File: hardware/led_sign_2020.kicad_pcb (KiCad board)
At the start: 2 copper layers, 70 x 86 mm, 30 parts, among them Q1 STD26P3LLH6, U1 ESP32-DevKitC, U2 MC74VHC1GT125, U3 MC74VHC1GT125, U4 MAX17601, U5 MAX17601, U6 MAX17601, U7 MAX17601

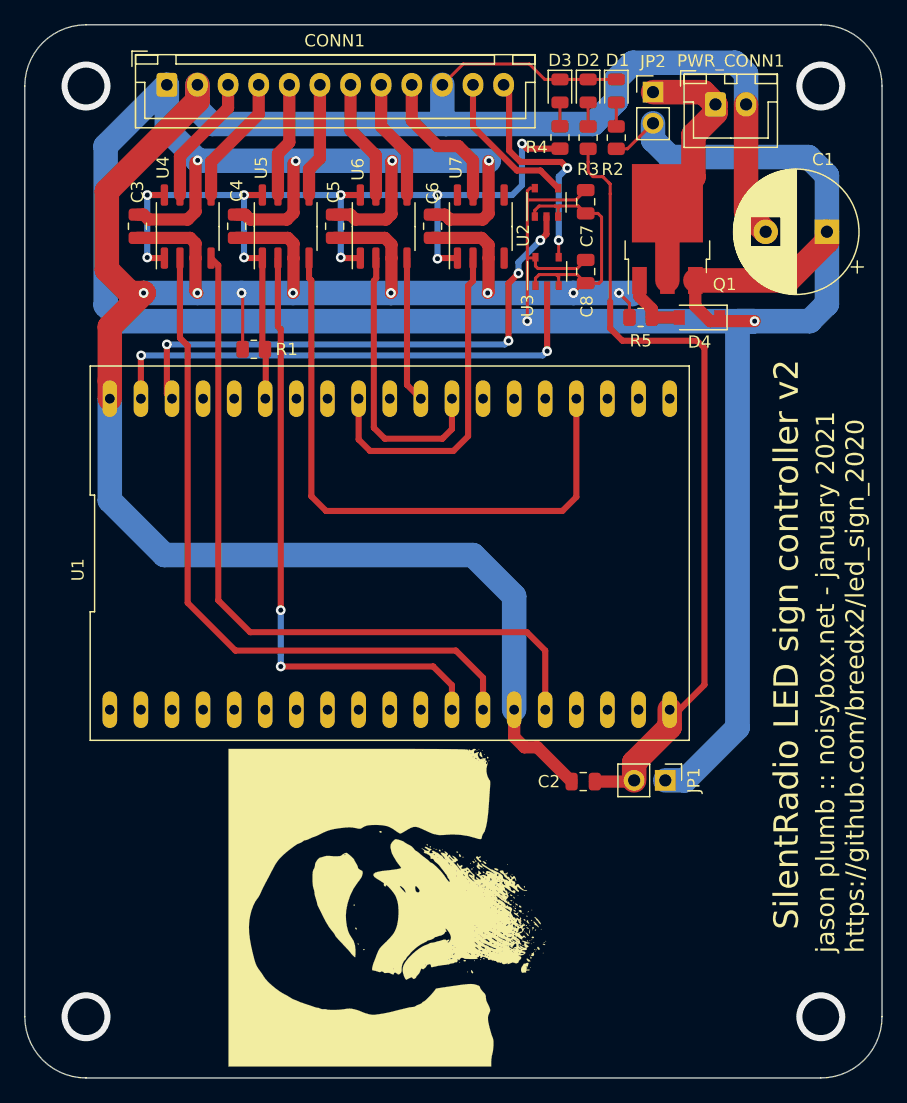
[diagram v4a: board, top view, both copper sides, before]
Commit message: add test point and silk notes
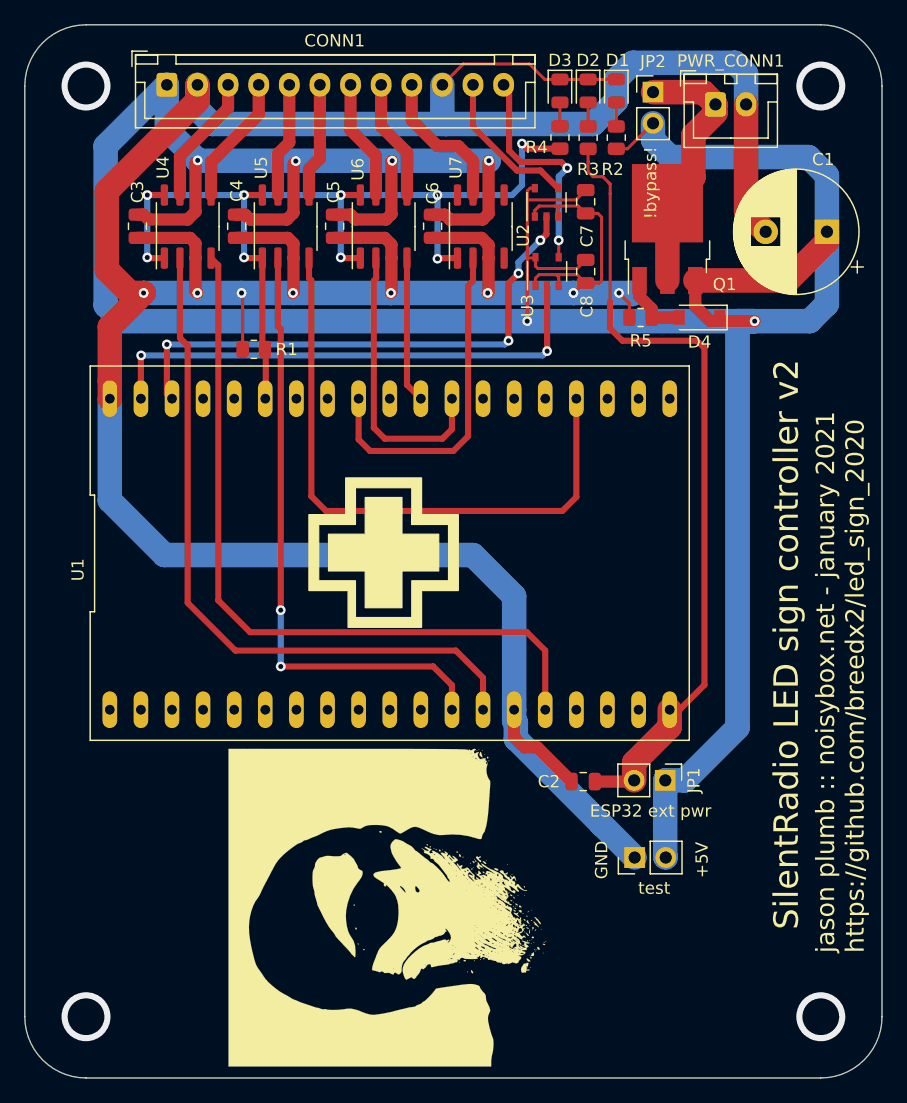
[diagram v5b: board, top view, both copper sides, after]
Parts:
- added test: PinHeader_1x02_P2.54mm_Vertical, Connector_PinHeader_2.54mm:PinHeader_1x02_P2.54mm_Vertical, F.Cu at (124.8, 123.0)
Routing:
- net GND: track 281.0 -> 297.2 mm
- net +5V: track 266.0 -> 272.3 mm
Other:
- board text added: "!bypass!"
- board text added: "+5V"
- board text added: "ESP32 ext pwr"
- board text added: "GND"
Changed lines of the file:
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@@
   (general
     (thickness 1.6)
-    (drawings 10)
-    (tracks 358)
+    (drawings 17)
+    (tracks 365)
     (zones 0)
-    (modules 30)
+    (modules 31)
     (nets 28)
   )
   (page A4)
   (layers
-    (0 F.Cu signal)
-    (31 B.Cu signal)
+    (0 F.Cu signal hide)
+    (31 B.Cu signal hide)
     (32 B.Adhes user)
     (33 F.Adhes user)
@@
     (38 B.Mask user)
     (39 F.Mask user)
-    (40 Dwgs.User user hide)
+    (40 Dwgs.User user)
     (41 Cmts.User user)
     (42 Eco1.User user)
@@
   )
   (setup
-    (last_trace_width 0.25)
+    (last_trace_width 2)
     (user_trace_width 0.25)
     (user_trace_width 0.5)
@@
     (mod_text_size 1 1)
     (mod_text_width 0.15)
-    (pad_size 1.524 1.524)
-    (pad_drill 0.762)
+    (pad_size 1.7 1.7)
+    (pad_drill 1)
     (pad_to_mask_clearance 0.0508)
     (solder_mask_min_width 0.101)
@@
     (add_net "Net-(D4-Pad2)")
     (add_net "Net-(JP2-Pad1)")
+  )
+  (module Connector_PinHeader_2.54mm:PinHeader_1x02_P2.54mm_Vertical (layer F.Cu)
+    (at 124.8 123 90)
+    (descr "Through hole straight pin header, 1x02, 2.54mm pitch, single row")
+    (tags "Through hole pin header THT 1x02 2.54mm single row")
+    (fp_text reference test (at -2.5 1.6 180) (layer F.SilkS)
+      (effects (font (size 1 1) (thickness 0.15)))
+    )
+    (fp_text value PinHeader_1x02_P2.54mm_Vertical (at 0 4.87 90) (layer F.Fab)
+      (effects (font (size 1 1) (thickness 0.15)))
+    )
+    (fp_line (start 1.8 -1.8) (end -1.8 -1.8) (layer F.CrtYd) (width 0.05))
+    (fp_line (start 1.8 4.35) (end 1.8 -1.8) (layer F.CrtYd) (width 0.05))
+    (fp_line (start -1.8 4.35) (end 1.8 4.35) (layer F.CrtYd) (width 0.05))
+    (fp_line (start -1.8 -1.8) (end -1.8 4.35) (layer F.CrtYd) (width 0.05))
+    (fp_line (start -1.33 -1.33) (end 0 -1.33) (layer F.SilkS) (width 0.12))
+    (fp_line (start -1.33 0) (end -1.33 -1.33) (layer F.SilkS) (width 0.12))
+    (fp_line (start -1.33 1.27) (end 1.33 1.27) (layer F.SilkS) (width 0.12))
+    (fp_line (start 1.33 1.27) (end 1.33 3.87) (layer F.SilkS) (width 0.12))
+    (fp_line (start -1.33 1.27) (end -1.33 3.87) (layer F.SilkS) (width 0.12))
+    (fp_line (start -1.33 3.87) (end 1.33 3.87) (layer F.SilkS) (width 0.12))
+    (fp_line (start -1.27 -0.635) (end -0.635 -1.27) (layer F.Fab) (width 0.1))
+    (fp_line (start -1.27 3.81) (end -1.27 -0.635) (layer F.Fab) (width 0.1))
+    (fp_line (start 1.27 3.81) (end -1.27 3.81) (layer F.Fab) (width 0.1))
+    (fp_line (start 1.27 -1.27) (end 1.27 3.81) (layer F.Fab) (width 0.1))
+    (fp_line (start -0.635 -1.27) (end 1.27 -1.27) (layer F.Fab) (width 0.1))
+    (fp_text user %R (at 0 1.27) (layer F.Fab)
+      (effects (font (size 1 1) (thickness 0.15)))
+    )
+    (pad 2 thru_hole oval (at 0 2.54 90) (size 1.7 1.7) (drill 1) (layers *.Cu *.Mask)
+      (net 2 +5V))
+    (pad 1 thru_hole rect (at 0 0 90) (size 1.7 1.7) (drill 1) (layers *.Cu *.Mask)
+      (net 1 GND))
+    (model ${KISYS3DMOD}/Connector_PinHeader_2.54mm.3dshapes/PinHeader_1x02_P2.54mm_Vertical.wrl
+      (at (xyz 0 0 0))
+      (scale (xyz 1 1 1))
+      (rotate (xyz 0 0 0))
+    )
   )
   (module custom:breedx_avatar (layer F.Cu)
@@
     )
   )
+  (gr_poly (pts (xy 110.4 95.8) (xy 106.6 95.8) (xy 106.6 95) (xy 110.4 95)) (layer F.SilkS) (width 0.1))
+  (gr_poly (pts (xy 107.4 95.8) (xy 106.6 95.8) (xy 106.6 92.8) (xy 102 92.8) (xy 102 95.8) (xy 99 95.8) (xy 99 100.4) (xy 102 100.4) (xy 102 103.4) (xy 106.6 103.4) (xy 106.6 100.4) (xy 109.6 100.4) (xy 109.6 95.8) (xy 110.4 95.8) (xy 110.4 101.2) (xy 107.4 101.2) (xy 107.4 104.2) (xy 101.4 104.2) (xy 101.4 101.2) (xy 98.2 101.2) (xy 98.2 95) (xy 101.2 95) (xy 101.2 92) (xy 107.4 92)) (layer F.SilkS) (width 0.1))
+  (gr_poly (pts (xy 105.8 96.6) (xy 108.8 96.6) (xy 108.8 99.6) (xy 105.8 99.6) (xy 105.8 102.6) (xy 102.8 102.6) (xy 102.8 99.6) (xy 99.8 99.6) (xy 99.8 96.6) (xy 102.8 96.6) (xy 102.8 93.6) (xy 105.8 93.6)) (layer F.SilkS) (width 0.1))
+  (gr_text !bypass! (at 126.1 67.9 90) (layer F.SilkS)
+    (effects (font (size 1 1) (thickness 0.15)))
+  )
+  (gr_text "ESP32 ext pwr" (at 126.1 119.2) (layer F.SilkS)
+    (effects (font (size 1 1) (thickness 0.15)))
+  )
+  (gr_text GND (at 122.1 123.2 90) (layer F.SilkS)
+    (effects (font (size 1 1) (thickness 0.15)))
+  )
+  (gr_text +5V (at 130.3 123.2 90) (layer F.SilkS)
+    (effects (font (size 1 1) (thickness 0.15)))
+  )
   (gr_text "jason plumb :: noisybox.net - january 2021\nhttps://github.com/breedx2/led_sign_2020\n" (at 141.6 130.8 90) (layer F.SilkS)
     (effects (font (size 1.5 1.5) (thickness 0.15)) (justify left))
@@
   (segment (start 118.55 70.66) (end 118.55 69.919998) (width 0.25) (layer F.Cu) (net 1))
   (segment (start 118.3 69.8) (end 118.669998 69.8) (width 0.25) (layer F.Cu) (net 1))
+  (segment (start 122.1 120.3) (end 124.8 123) (width 2) (layer B.Cu) (net 1))
+  (segment (start 115.1 113.3) (end 122.1 120.3) (width 2) (layer B.Cu) (net 1))
+  (segment (start 115.1 111.975598) (end 115.1 113.3) (width 2) (layer B.Cu) (net 1))
+  (segment (start 114.96 111.835598) (end 115.1 111.975598) (width 2) (layer B.Cu) (net 1))
+  (segment (start 114.96 110.93) (end 114.96 111.835598) (width 2) (layer B.Cu) (net 1))
   (segment (start 88.9 68.94) (end 88.94 68.9) (width 0.5) (layer F.Cu) (net 2))
   (via (at 112.9 66.1) (size 0.8) (drill 0.4) (layers F.Cu B.Cu) (net 2))
@@
   (segment (start 129.755 77.975) (end 130.98 79.2) (width 1) (layer F.Cu) (net 2))
   (segment (start 129.755 75.875) (end 129.755 77.975) (width 1) (layer F.Cu) (net 2))
+  (segment (start 127.3 122.96) (end 127.34 123) (width 2) (layer B.Cu) (net 2))
+  (segment (start 127.3 116.7) (end 127.3 122.96) (width 2) (layer B.Cu) (net 2))
   (segment (start 123.3 61.3375) (end 123.3 63.3) (width 0.25) (layer F.Cu) (net 3))
   (segment (start 121 61.3375) (end 121 63.3) (width 0.25) (layer F.Cu) (net 4))
